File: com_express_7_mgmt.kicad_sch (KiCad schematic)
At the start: 77 parts, among them J12 Plug_Bus_CE7_EPT_401-51501-51, J13 PinHeader_1x3_P2.54mm_Drill1.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, J14 PinHeader_1x3_P2.54mm_Drill1.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, Q11 BSS138-7-F, Q12 BSS138-7-F, SW1 SW_1-1825027-1_THT, U30 74AUP2G132, U31 M24C64-F_DFN8, U32 TPS3840PL30DBVR, U33 74AUP2G132, U34 LTC2950CTS8-1, U36 W25Q32FV_SOIC-8

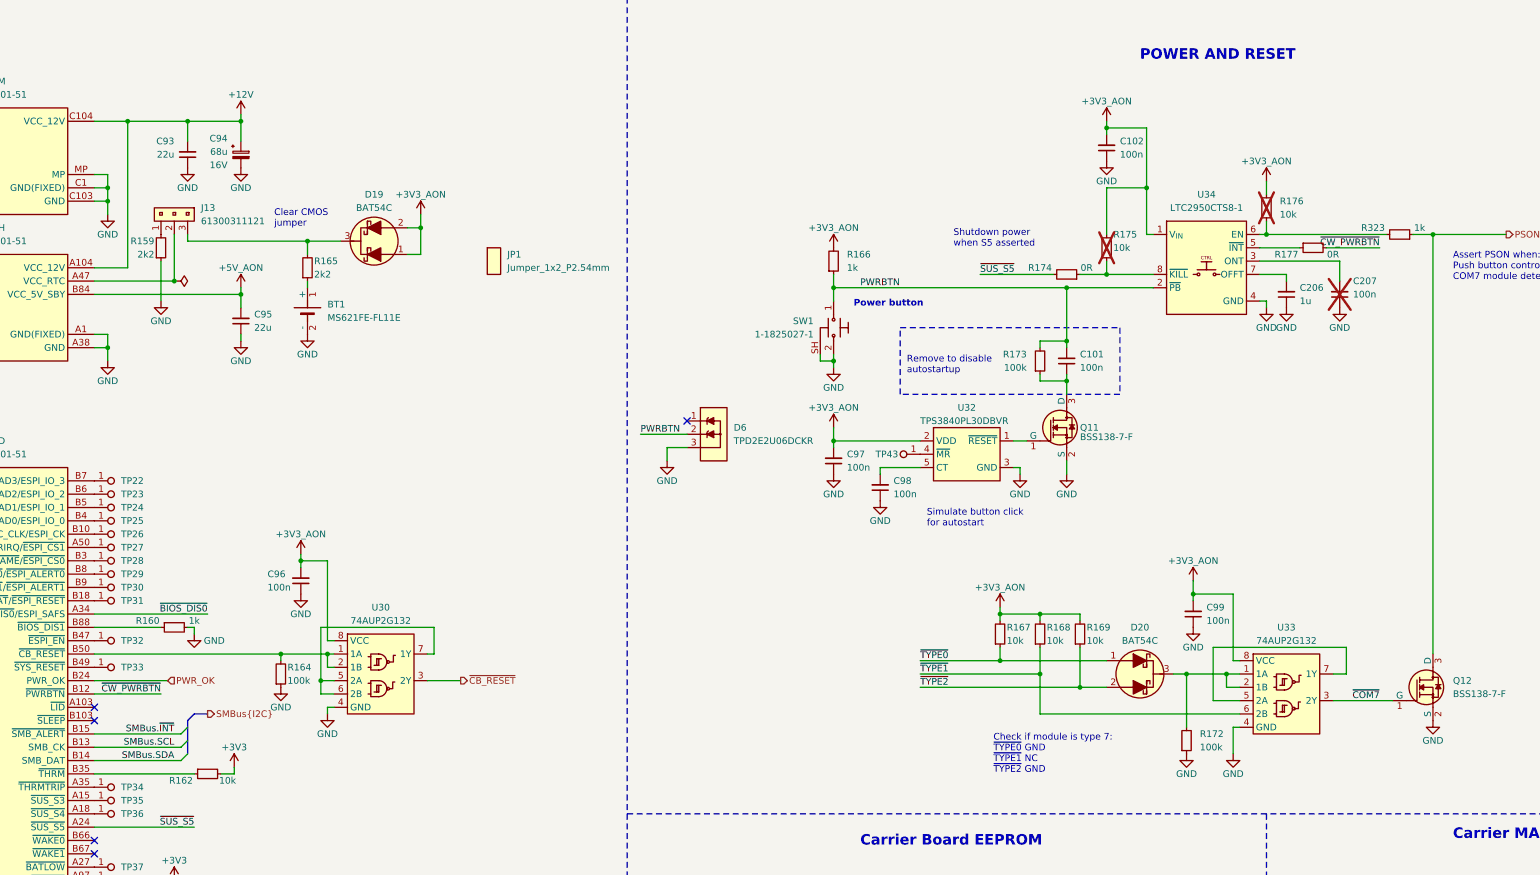
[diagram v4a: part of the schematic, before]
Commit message: [#66613] Fix ERC, adjust overlapping text on schematic
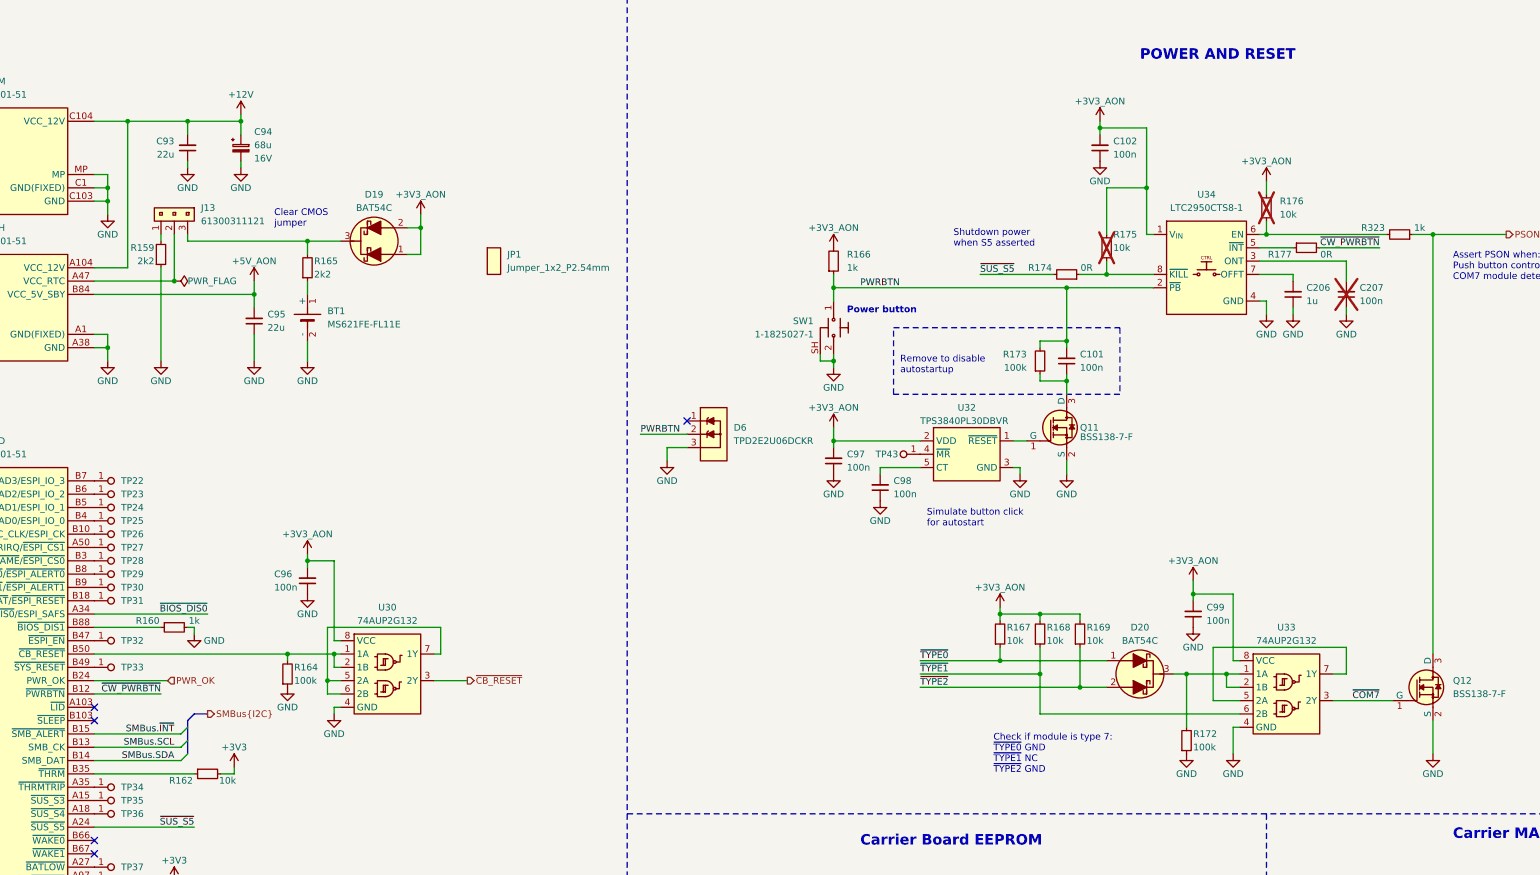
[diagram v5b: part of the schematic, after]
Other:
- moved on the sheet: BT1, C102, C206, C207, C93, C94, C95, C96, R159, R164, R177, U30
